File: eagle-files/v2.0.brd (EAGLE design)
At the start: 39.4 x 77.5 mm, 37 parts, among them U2 MLX90614_

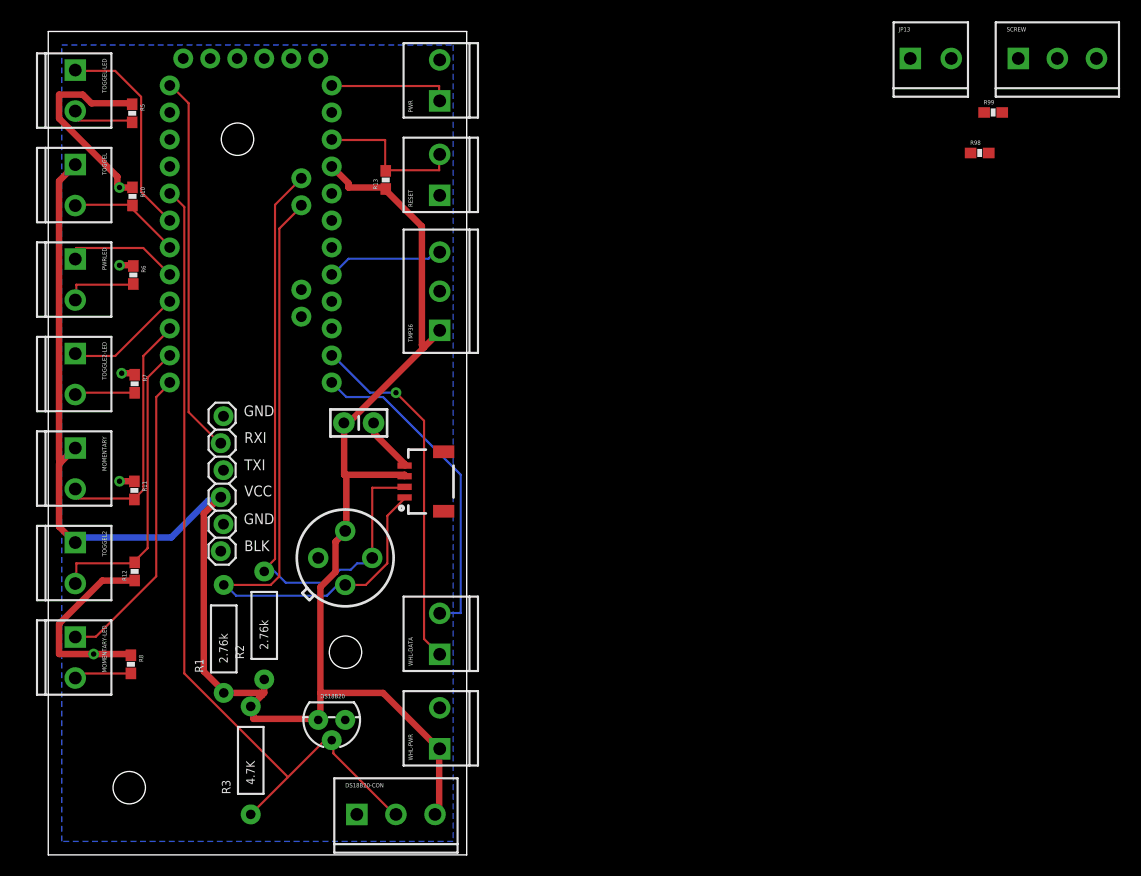
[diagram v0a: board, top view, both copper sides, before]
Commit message: Fixed a bunch of errors with the eagle schematic. SLC and SDA were mixed up.
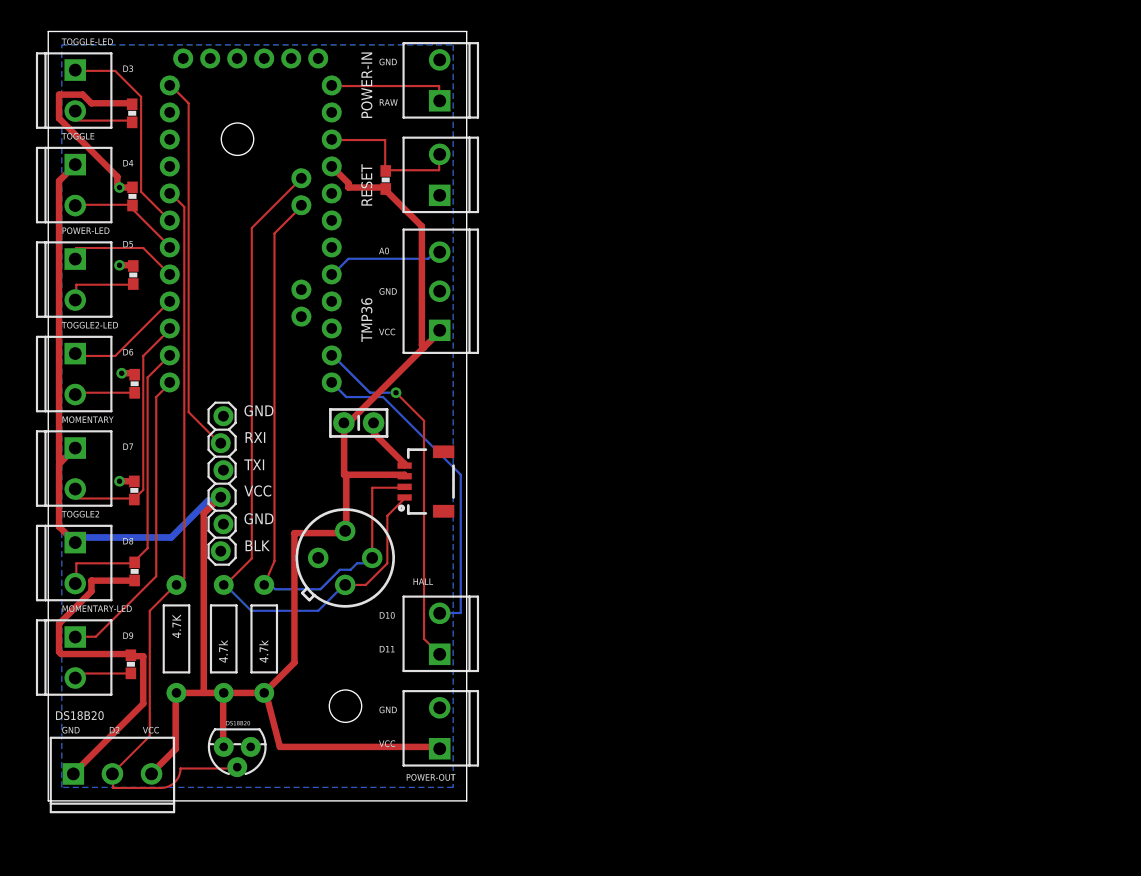
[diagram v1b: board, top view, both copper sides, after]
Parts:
- removed JP13: M023.5MM_LOCK, SparkFun-Connectors:SCREWTERMINAL-3.5MM-2_LOCK
- removed JP8: STAND-OFFTIGHT, SparkFun:STAND-OFF-TIGHT
- removed R98: 10K, SparkFun-Resistors:0603-RES
- removed R99: 330, SparkFun-Resistors:0603-RES
- removed SCREW: (no value), SparkFun-Connectors:SCREWTERMINAL-3.5MM-3_LOCK.007S
- R1, R2: value 2.76k -> 4.7k
- moved DS18B20-CON 26.9 mm to (2.54, 7.62)
- moved R3 13.4 mm to (12.1, 20.3), turned to 270 degrees
- moved DS18B20 9.25 mm to (17.8, 10.2)
- moved JP6 5.08 mm to (28.0, 14.0)
- moved R2 1.27 mm to (20.3, 20.3)
- renumbered WHL-DATA to DIG10/11, WHL-PWR to VCC/GND
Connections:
- net N$21: now also PRO_MINI.A4; no longer PRO_MINI.A5
- net N$22: now also PRO_MINI.A5; no longer PRO_MINI.A4
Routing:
- net GND: track 47.4 -> 62.8 mm, vias 5 -> 4
- net 5V: track 178.6 -> 188.5 mm
- net N$2: track 79.7 -> 72.0 mm
- net N$21: track 60.0 -> 58.3 mm
- net N$22: track 65.3 -> 66.5 mm
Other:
- board size 39.4 x 77.5 mm -> 39.4 x 72.4 mm
- board text added: "A0"
- board text added: "D10"
- board text added: "D11"
- board text added: "D2"
- board text added: "D3"
- board text added: "D4"
- board text added: "D5"
- board text added: "D6"
- board text added: "D7"
- board text added: "D8"
- board text added: "D9"
- board text added: "DS18B20"
- board text added: "HALL"
- board text added: "MOMENTARY"
- board text added: "MOMENTARY-LED"
- board text added: "POWER-IN"
- board text added: "POWER-LED"
- board text added: "POWER-OUT"
- board text added: "RAW"
- board text added: "RESET"
- board text added: "TMP36"
- board text added: "TOGGLE"
- board text added: "TOGGLE-LED"
- board text added: "TOGGLE2"
- board text added: "TOGGLE2-LED"

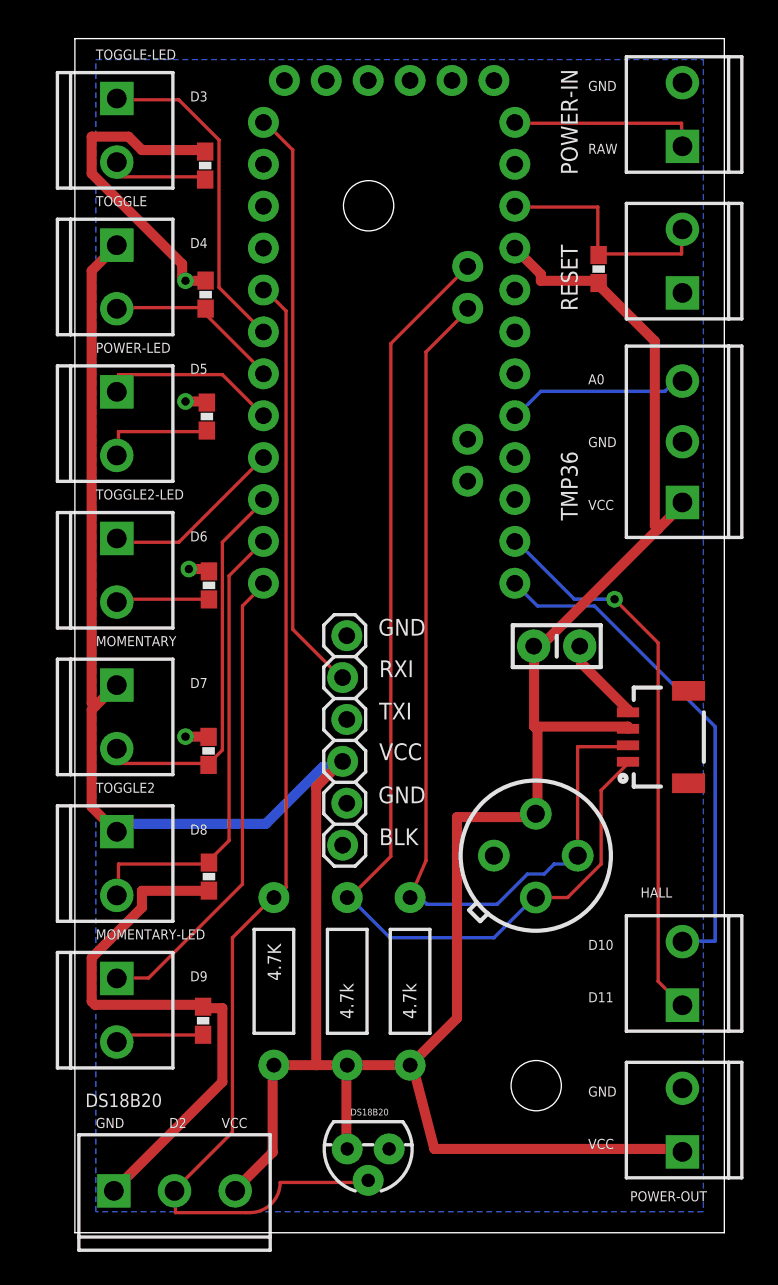
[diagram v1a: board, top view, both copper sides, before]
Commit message: Played with the eagle board and cleaned it up. Made clearances 12mil for everything.
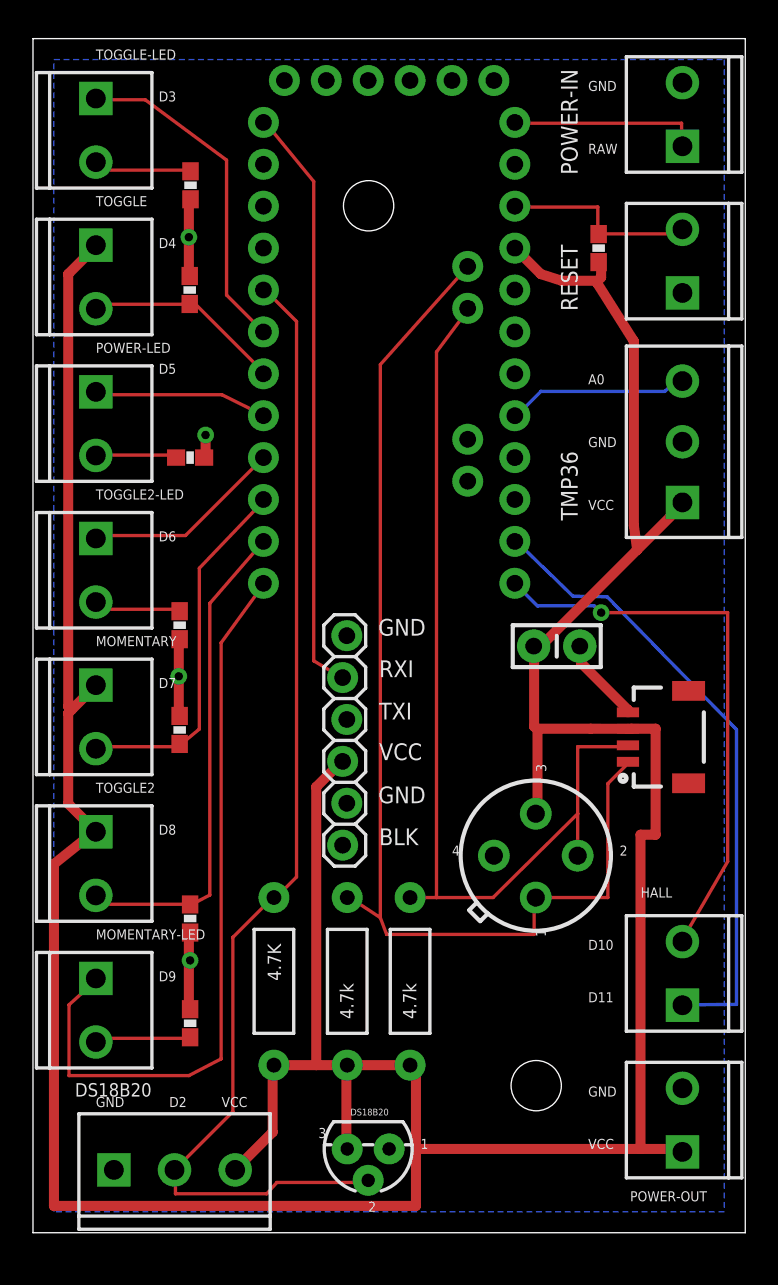
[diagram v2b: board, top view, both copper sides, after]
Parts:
- TMP36: value (none) -> TMP36
- moved R7 3.00 mm to (6.35, 41.9), turned to 90 degrees
- moved R12 2.79 mm to (6.99, 24.1)
- moved R6 2.69 mm to (6.99, 52.1), turned to 180 degrees
- moved R11 2.16 mm to (6.35, 35.6)
- moved R5 1.49 mm to (7.01, 68.6), turned to 90 degrees
- moved DS18B20-CON 1.27 mm to (2.54, 8.89)
- moved MOMENTARY 1.27 mm to (1.27, 38.1)
- moved MOMENTARY-LED 1.27 mm to (1.27, 20.3)
- moved PWRLED 1.27 mm to (1.27, 55.9)
- moved TOGGEL 1.27 mm to (1.27, 64.8)
- moved TOGGEL-LED 1.27 mm to (1.27, 73.7)
- moved TOGGEL2 1.27 mm to (1.27, 29.2)
- moved TOGGLE2-LED 1.27 mm to (1.27, 47.0)
- moved R13 1.27 mm to (31.8, 64.8)
- moved R10 1.00 mm to (6.96, 62.2)
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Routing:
- net 5V: track 188.5 -> 230.9 mm
- net GND: track 62.8 -> 20.8 mm
- net N$17: track 28.7 -> 45.7 mm
- net N$3: track 33.8 -> 38.1 mm, vias 1 -> 0
- net N$11: track 30.7 -> 34.4 mm, vias 0 -> 1
- net N$22: track 66.5 -> 69.3 mm
- net N$19: track 14.5 -> 12.0 mm
- net N$14: track 6.91 -> 4.98 mm
- net N$18: track 28.4 -> 30.2 mm
- net N$10: track 23.9 -> 22.2 mm
- net N$1: track 10.9 -> 12.3 mm
- net N$2: track 72.0 -> 70.9 mm
- net N$13: track 11.2 -> 12.2 mm
- net N$12: track 20.0 -> 20.5 mm
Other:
- board size 39.4 x 72.4 mm -> 43.2 x 72.4 mm
- board text added: "1"
- board text added: "2"
- board text added: "3"
- board text added: "4"
- board text added: "MOMEN TARY"
- board text added: "MOMENT ARY LED"
- board text added: "POWER IN"
- board text added: "POWER LED"
- board text added: "POWER OUT"
- board text added: "TOGGLE LED"
- board text added: "TOGGLE2 LED"
